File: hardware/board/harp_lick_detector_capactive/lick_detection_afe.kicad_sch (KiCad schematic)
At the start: 77 parts, among them J3 Conn_Triaxial, U10 ADA4891-2, U13 ADS7049, U14 MAX4564EKA, U15 MAX4564EKA, U6 ADA4891-4, U7 LTC6268xS8-10, U8 REF2025, U9 TS5A9411DCKR

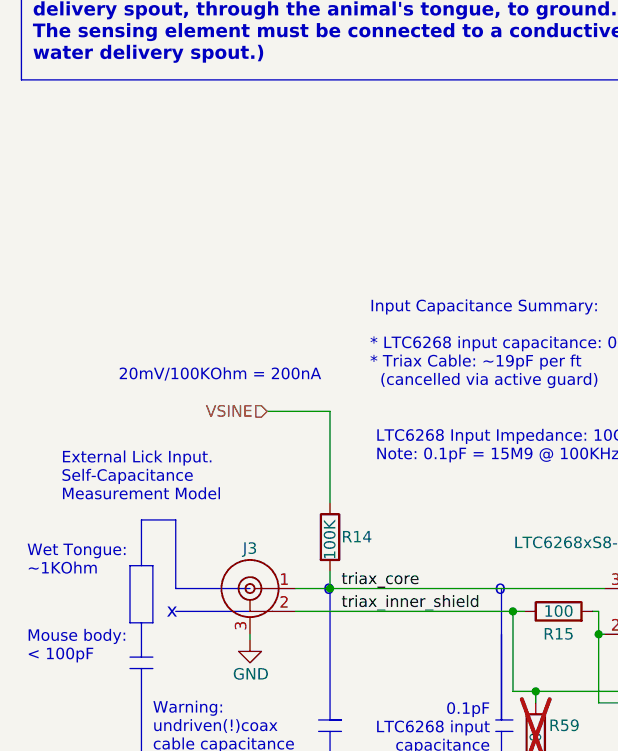
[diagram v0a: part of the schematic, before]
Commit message: add cable drawing
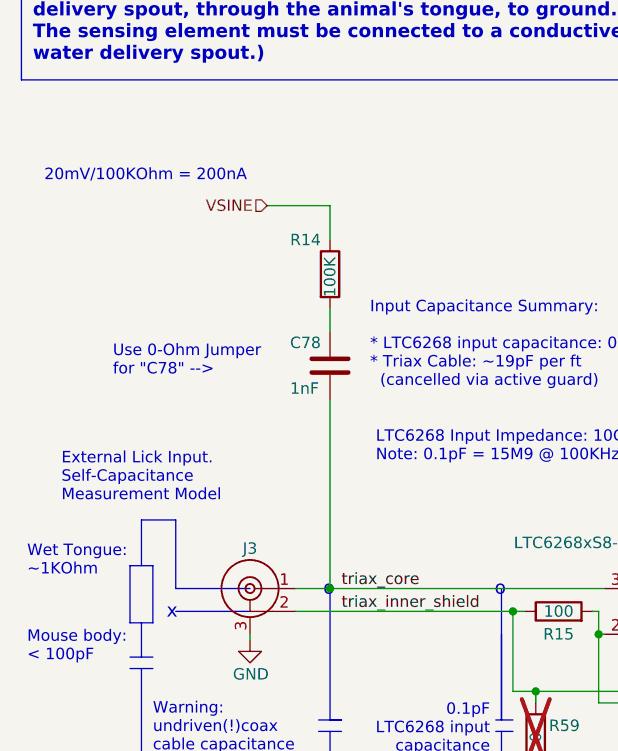
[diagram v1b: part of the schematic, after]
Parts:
- added C78: 1nF, Resistor_SMD:R_1206_3216Metric, symbol Device:C
- J3: Alternate (none) -> CBBJR79
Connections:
- net triax_core: now also C78.2; no longer R14.2
- new net: C78.1, R14.2
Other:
- note added: "Use 0-Ohm Jumper for "C78" -->"
- moved on the sheet: R14
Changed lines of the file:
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@@
 	)
 	(junction
+		(at 47.625 94.615)
+		(diameter 0)
+		(color 0 0 0 0)
+	)
+	(junction
 		(at 70.485 106.045)
 		(diameter 0)
@@
 	)
 	(junction
-		(at 47.625 94.615)
-		(diameter 0)
-		(color 0 0 0 0)
-	)
-	(junction
 		(at 109.22 58.42)
 		(diameter 0)
@@
 	(wire
 		(pts
-			(xy 47.625 74.93) (xy 47.625 85.09)
+			(xy 47.625 52.07) (xy 47.625 55.88)
 		)
 		(stroke
@@
 	(wire
 		(pts
-			(xy 47.625 92.71) (xy 47.625 94.615)
-		)
-		(stroke
-			(width 0)
-			(type default)
-		)
-	)
-	(wire
-		(pts
 			(xy 109.22 69.215) (xy 107.95 69.215)
 		)
@@
 	(wire
 		(pts
+			(xy 47.625 63.5) (xy 47.625 66.04)
+		)
+		(stroke
+			(width 0)
+			(type default)
+		)
+	)
+	(wire
+		(pts
 			(xy 134.62 58.42) (xy 133.35 58.42)
 		)
@@
 	(wire
 		(pts
+			(xy 47.625 73.66) (xy 47.625 94.615)
+		)
+		(stroke
+			(width 0)
+			(type default)
+		)
+	)
+	(wire
+		(pts
 			(xy 143.51 104.775) (xy 143.51 106.045)
 		)
@@
 	(wire
 		(pts
+			(xy 47.625 94.615) (xy 78.105 94.615)
+		)
+		(stroke
+			(width 0)
+			(type default)
+		)
+	)
+	(wire
+		(pts
 			(xy 70.485 114.935) (xy 70.485 116.205)
 		)
@@
 	(wire
 		(pts
-			(xy 47.625 94.615) (xy 78.105 94.615)
-		)
-		(stroke
-			(width 0)
-			(type default)
-		)
-	)
-	(wire
-		(pts
 			(xy 211.455 104.14) (xy 212.09 104.14)
 		)
@@
 	(wire
 		(pts
-			(xy 40.64 74.93) (xy 47.625 74.93)
+			(xy 40.64 52.07) (xy 47.625 52.07)
 		)
 		(stroke
@@
 	(text "20mV/100KOhm = 200nA"
 		(exclude_from_sim no)
-		(at 24.13 71.755 0)
+		(at 15.875 49.53 0)
 		(effects
 			(font
@@
 		)
 	)
+	(text "Use 0-Ohm Jumper\nfor \"C78\" -->"
+		(exclude_from_sim no)
+		(at 23.495 71.12 0)
+		(effects
+			(font
+				(size 1.27 1.27)
+			)
+			(justify left bottom)
+		)
+	)
 	(text "Mouse body:\n< 100pF"
 		(exclude_from_sim no)
@@
 	(hierarchical_label "VSINE"
 		(shape input)
-		(at 40.64 74.93 180)
+		(at 40.64 52.07 180)
 		(fields_autoplaced yes)
 		(effects
@@
 			)
 		)
+		(property "Alternate" "CBBJR79"
+			(at 38.735 94.615 0)
+			(effects
+				(font
+					(size 1.27 1.27)
+				)
+				(hide yes)
+			)
+		)
 		(pin "1"
 		)
@@
 	)
 	(symbol
+		(lib_id "Device:C")
+		(at 47.625 69.85 0)
+		(unit 1)
+		(exclude_from_sim no)
+		(in_bom yes)
+		(on_board yes)
+		(dnp no)
+		(property "Reference" "C78"
+			(at 43.18 67.31 0)
+			(effects
+				(font
+					(size 1.27 1.27)
+				)
+				(justify left)
+			)
+		)
+		(property "Value" "1nF"
+			(at 43.18 72.39 0)
+			(effects
+				(font
+					(size 1.27 1.27)
+				)
+				(justify left)
+			)
+		)
+		(property "Footprint" "Resistor_SMD:R_1206_3216Metric"
+			(at 48.5902 73.66 0)
+			(effects
+				(font
+					(size 1.27 1.27)
+				)
+				(hide yes)
+			)
+		)
+		(property "Datasheet" "https://www.yageo.com/upload/media/product/products/datasheet/rchip/PYu-RC_Group_51_RoHS_L_12.pdf"
+			(at 47.625 69.85 0)
+			(effects
+				(font
+					(size 1.27 1.27)
+				)
+				(hide yes)
+			)
+		)
+		(property "Description" "0-Ohm Resistor."
+			(at 47.625 69.85 0)
+			(effects
+				(font
+					(size 1.27 1.27)
+				)
+				(hide yes)
+			)
+		)
+		(property "Manufacturer Number" "KGM31BCG1H102FT"
+			(at 47.625 69.85 0)
+			(effects
+				(font
+					(size 1.27 1.27)
+				)
+				(hide yes)
+			)
+		)
+		(property "Manufacturer" "Yageo"
+			(at 47.625 69.85 0)
+			(effects
+				(font
+					(size 1.27 1.27)
+				)
+				(hide yes)
+			)
+		)
+		(property "Notes" "Short w/0-Ohm Resistor by default. Use KGM31BCG1H102FT if required."
+			(at 47.625 69.85 0)
+			(effects
+				(font
+					(size 1.27 1.27)
+				)
+				(hide yes)
+			)
+		)
+		(pin "2"
+		)
+		(pin "1"
+		)
+		(instances
+			(project ""
+				(path "/e63e39d7-6ac0-4ffd-8aa3-1841a4541b55/8b2c79bc-d662-4528-ac6e-e4616ba8e8ad"
+					(reference "C78")
+					(unit 1)
+				)
+			)
+		)
+	)
+	(symbol
 		(lib_id "power:GND")
 		(at 127 137.795 0)
@@
 	(symbol
 		(lib_id "Device:R")
-		(at 47.625 88.9 0)
+		(at 47.625 59.69 0)
 		(unit 1)
 		(exclude_from_sim no)
@@
 		(dnp no)
 		(property "Reference" "R14"
-			(at 48.895 88.9 0)
+			(at 43.18 55.88 0)
 			(effects
 				(font
@@
 		)
 		(property "Value" "100K"
-			(at 47.625 91.44 90)
+			(at 47.625 62.23 90)
 			(effects
 				(font
@@
 		)
 		(property "Footprint" "Resistor_SMD:R_1206_3216Metric"
-			(at 45.847 88.9 90)
+			(at 45.847 59.69 90)
 			(effects
 				(font
@@
 		)
 		(property "Datasheet" "n/a"
-			(at 47.625 88.9 0)
+			(at 47.625 59.69 0)
 			(effects
 				(font
@@
 		)
 		(property "Description" ""
-			(at 47.625 88.9 0)
+			(at 47.625 59.69 0)
 			(effects
 				(font
@@
 		)
 		(property "Link" "https://www.digikey.com/en/products/detail/yageo/RT1206FRE07100KL/1082857"
-			(at 47.625 88.9 0)
+			(at 47.625 59.69 0)
 			(effects
 				(font
@@
 		)
 		(property "Manufacturer" "Yageo"
-			(at 47.625 88.9 0)
+			(at 47.625 59.69 0)
 			(effects
 				(font
@@
 		)
 		(property "Manufacturer Number" "RT1206FRE07100KL"
-			(at 47.625 88.9 0)
+			(at 47.625 59.69 0)
 			(effects
 				(font
@@
 		)
 		(property "Tolerance" "1%"
-			(at 47.625 88.9 0)
+			(at 47.625 59.69 0)
 			(effects
 				(font
@@
 		)
 		(property "Notes" ""
-			(at 47.625 88.9 0)
+			(at 47.625 59.69 0)
 			(effects
 				(font

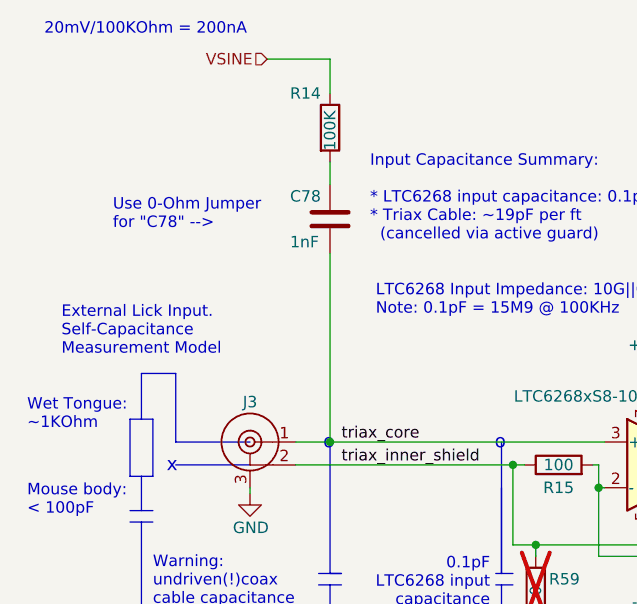
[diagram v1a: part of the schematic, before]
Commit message: undo series capacitor additions (unfinished change)
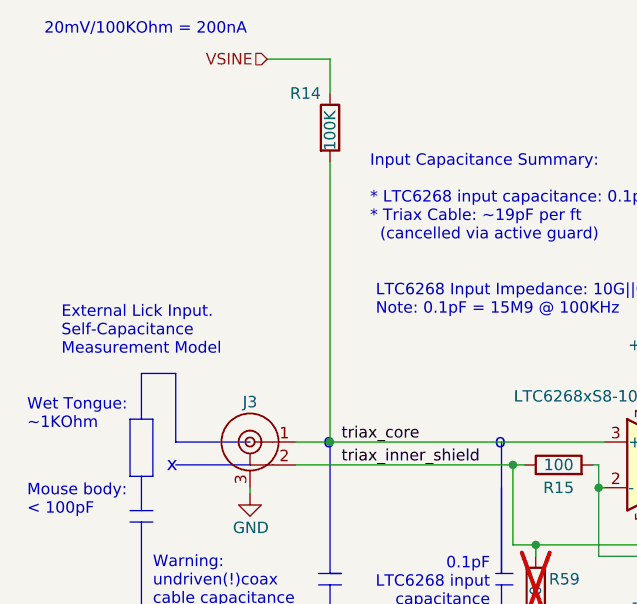
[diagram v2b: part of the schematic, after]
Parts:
- removed C78: 1nF, Resistor_SMD:R_1206_3216Metric, symbol Device:C
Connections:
- net triax_core: now also R14.2
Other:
- note removed: "Use 0-Ohm Jumper for "C78" -->"
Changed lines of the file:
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@@
 	(wire
 		(pts
-			(xy 47.625 63.5) (xy 47.625 66.04)
-		)
-		(stroke
-			(width 0)
-			(type default)
-		)
-	)
-	(wire
-		(pts
 			(xy 134.62 58.42) (xy 133.35 58.42)
 		)
@@
 	(wire
 		(pts
-			(xy 47.625 73.66) (xy 47.625 94.615)
+			(xy 47.625 63.5) (xy 47.625 94.615)
 		)
 		(stroke
@@
 		)
 	)
-	(text "Use 0-Ohm Jumper\nfor \"C78\" -->"
-		(exclude_from_sim no)
-		(at 23.495 71.12 0)
-		(effects
-			(font
-				(size 1.27 1.27)
-			)
-			(justify left bottom)
-		)
-	)
 	(text "Mouse body:\n< 100pF"
 		(exclude_from_sim no)
@@
 					(unit 1)
 				)
-			)
-		)
-	)
-	(symbol
-		(lib_id "Device:C")
-		(at 47.625 69.85 0)
-		(unit 1)
-		(exclude_from_sim no)
-		(in_bom yes)
-		(on_board yes)
-		(dnp no)
-		(property "Reference" "C78"
-			(at 43.18 67.31 0)
-			(effects
-				(font
-					(size 1.27 1.27)
-				)
-				(justify left)
-			)
-		)
-		(property "Value" "1nF"
-			(at 43.18 72.39 0)
-			(effects
-				(font
-					(size 1.27 1.27)
-				)
-				(justify left)
-			)
-		)
-		(property "Footprint" "Resistor_SMD:R_1206_3216Metric"
-			(at 48.5902 73.66 0)
-			(effects
-				(font
-					(size 1.27 1.27)
-				)
-				(hide yes)
-			)
-		)
-		(property "Datasheet" "https://www.yageo.com/upload/media/product/products/datasheet/rchip/PYu-RC_Group_51_RoHS_L_12.pdf"
-			(at 47.625 69.85 0)
-			(effects
-				(font
-					(size 1.27 1.27)
-				)
-				(hide yes)
-			)
-		)
-		(property "Description" "0-Ohm Resistor."
-			(at 47.625 69.85 0)
-			(effects
-				(font
-					(size 1.27 1.27)
-				)
-				(hide yes)
-			)
-		)
-		(property "Manufacturer Number" "KGM31BCG1H102FT"
-			(at 47.625 69.85 0)
-			(effects
-				(font
-					(size 1.27 1.27)
-				)
-				(hide yes)
-			)
-		)
-		(property "Manufacturer" "Yageo"
-			(at 47.625 69.85 0)
-			(effects
-				(font
-					(size 1.27 1.27)
-				)
-				(hide yes)
-			)
-		)
-		(property "Notes" "Short w/0-Ohm Resistor by default. Use KGM31BCG1H102FT if required."
-			(at 47.625 69.85 0)
-			(effects
-				(font
-					(size 1.27 1.27)
-				)
-				(hide yes)
-			)
-		)
-		(pin "2"
-		)
-		(pin "1"
-		)
-		(instances
-			(project ""
-				(path "/e63e39d7-6ac0-4ffd-8aa3-1841a4541b55/8b2c79bc-d662-4528-ac6e-e4616ba8e8ad"
-					(reference "C78")
-					(unit 1)
-				)
